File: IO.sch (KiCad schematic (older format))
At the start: 5 parts

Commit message: more updates
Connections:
- net Signaling-RINGING: no longer J?.R1
- new net Signaling-RINGDOWN: J?.R1
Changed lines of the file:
@@
 Baseband-IN
 Text GLabel 2450 2150 2    50   Output ~ 0
-Signaling-RINGING
+Signaling-RINGDOWN
 Text Notes 850  1050 0    50   ~ 0
 Audio Jack

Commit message: updates
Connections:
- net Signaling-RINGING is gone; now on net Signaling-RINGDOWN: J?.8 (Pin_8)
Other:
- note added: "Baseband Module Interface"
- note removed: "Module Interface"
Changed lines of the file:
@@
 $Descr A4 11693 8268
 encoding utf-8
-Sheet 6 10
+Sheet 6 11
 Title "300 Baud Audio FSK Modem "
 Date "2021-07-08"
@@
 	0    -1   -1   0
 $EndComp
-Text GLabel 7100 4450 2    50   Input ~ 0
+Text GLabel 7100 4450 2    50   Output ~ 0
 Baseband-IN
-Text GLabel 7100 4550 2    50   Output ~ 0
+Text GLabel 7100 4550 2    50   Input ~ 0
 Baseband-OUT
 Text GLabel 7100 4650 2    50   Input ~ 0
@@
 E&M-SG
 Text GLabel 7100 4350 2    50   Output ~ 0
-Signaling-RINGING
+Signaling-RINGDOWN
 $Comp
 L power:GND #PWR?
@@
 	1    0    0    -1
 $EndComp
-Text Notes 5200 4500 0    50   ~ 0
-Module Interface
+Text Notes 5000 4500 0    50   ~ 0
+Baseband Module Interface
 Text GLabel 2350 4450 2    50   Input ~ 0
 E&M-R

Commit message: updates
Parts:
- added J? (x2): AudioPlug4, symbol Connector:AudioPlug4
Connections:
- net Baseband-IN: now also J?.T
- net Baseband-OUT: now also J?.T
- net GND: now also J?.S, J?.S
- net Signaling-OFFHOOK: now also J?.R1
- net Signaling-RINGDOWN: now also J?.R1
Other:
- note added: "Crossover Cable Example"
- note removed: "Audio Jack"
- moved on the sheet: J?

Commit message: updates
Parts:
- J? (x2): symbol Connector:AudioPlug4 -> Connector:AudioPlug3
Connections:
- net Baseband-IN: now also J?.R, J?.R; no longer J?.T, J?.T
- net Baseband-OUT: now also J?.T; no longer J?.T
- net GND: now also J?.R2, J?.R2
- net Signaling-OFFHOOK: now also J?.T, J?.T; no longer J?.R1, J?.R1
- net Signaling-RINGDOWN: now also J?.R1; no longer J?.R1
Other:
- note added: "X"
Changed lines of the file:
@@
 RST_Request
 $Comp
-L Connector:AudioPlug4 J?
+L Connector:AudioPlug3 J?
 U 1 1 60EB32CF
-P 1850 1350
+P 1850 1400
 AR Path="/60EB32CF" Ref="J?"  Part="1"
 AR Path="/60E9D9E5/60EB32CF" Ref="J?"  Part="1"
-F 0 "J?" H 1907 1675 50  0000 C CNN
-F 1 "AudioPlug4" H 1907 1584 50  0000 C CNN
-F 2 "" H 2200 1250 50  0001 C CNN
-F 3 "~" H 2200 1250 50  0001 C CNN
-	1    1850 1350
+F 0 "J?" H 1907 1725 50  0000 C CNN
+F 1 "AudioPlug4" H 1907 1634 50  0000 C CNN
+F 2 "" H 2200 1300 50  0001 C CNN
+F 3 "~" H 2200 1300 50  0001 C CNN
+	1    1850 1400
 	1    0    0    -1
 $EndComp
@@
 L power:GND #PWR?
 U 1 1 60EB32D5
-P 2450 1250
+P 2450 1300
 AR Path="/60EB32D5" Ref="#PWR?"  Part="1"
 AR Path="/60E9D9E5/60EB32D5" Ref="#PWR?"  Part="1"
-F 0 "#PWR?" H 2450 1000 50  0001 C CNN
-F 1 "GND" V 2455 1122 50  0000 R CNN
-F 2 "" H 2450 1250 50  0001 C CNN
-F 3 "" H 2450 1250 50  0001 C CNN
-	1    2450 1250
-	0    -1   -1   0
-$EndComp
-Text GLabel 2450 1550 2    50   Output ~ 0
+F 0 "#PWR?" H 2450 1050 50  0001 C CNN
+F 1 "GND" V 2455 1172 50  0000 R CNN
+F 2 "" H 2450 1300 50  0001 C CNN
+F 3 "" H 2450 1300 50  0001 C CNN
+	1    2450 1300
+	0    -1   -1   0
+$EndComp
+Text GLabel 2450 1500 2    50   Output ~ 0
 Baseband-OUT
-Text GLabel 2450 1450 2    50   Output ~ 0
+Text GLabel 2450 2400 2    50   Output ~ 0
 Signaling-OFFHOOK
 Wire Notes Line
@@
 	8000 4250 3800 4250
 $Comp
-L Connector:AudioPlug4 J?
+L Connector:AudioPlug3 J?
 U 1 1 60EE43AB
-P 5900 1350
+P 5900 1400
 AR Path="/60EE43AB" Ref="J?"  Part="1"
 AR Path="/60E9D9E5/60EE43AB" Ref="J?"  Part="1"
-F 0 "J?" H 5957 1675 50  0000 C CNN
-F 1 "AudioPlug4" H 5957 1584 50  0000 C CNN
-F 2 "" H 6250 1250 50  0001 C CNN
-F 3 "~" H 6250 1250 50  0001 C CNN
-	1    5900 1350
+F 0 "J?" H 5957 1725 50  0000 C CNN
+F 1 "AudioPlug4" H 5957 1634 50  0000 C CNN
+F 2 "" H 6250 1300 50  0001 C CNN
+F 3 "~" H 6250 1300 50  0001 C CNN
+	1    5900 1400
 	-1   0    0    -1
 $EndComp
@@
 L power:GND #PWR?
 U 1 1 60EE44F5
-P 5300 1250
+P 5300 1300
 AR Path="/60EE44F5" Ref="#PWR?"  Part="1"
 AR Path="/60E9D9E5/60EE44F5" Ref="#PWR?"  Part="1"
-F 0 "#PWR?" H 5300 1000 50  0001 C CNN
-F 1 "GND" V 5305 1122 50  0000 R CNN
-F 2 "" H 5300 1250 50  0001 C CNN
-F 3 "" H 5300 1250 50  0001 C CNN
-	1    5300 1250
+F 0 "#PWR?" H 5300 1050 50  0001 C CNN
+F 1 "GND" V 5305 1172 50  0000 R CNN
+F 2 "" H 5300 1300 50  0001 C CNN
+F 3 "" H 5300 1300 50  0001 C CNN
+	1    5300 1300
 	0    1    -1   0
 $EndComp
-Text GLabel 5300 1550 0    50   Input ~ 0
+Text GLabel 5300 1400 0    50   Input ~ 0
 Baseband-IN
-Text GLabel 5300 1450 0    50   Input ~ 0
+Text GLabel 5300 2300 0    50   Input ~ 0
 Signaling-RINGDOWN
 Text Notes 3250 1000 0    50   ~ 0
@@
 	0    -1   -1   0
 $EndComp
+Text GLabel 5300 1500 0    50   Output ~ 0
+Baseband-OUT
 Text GLabel 5300 2400 0    50   Output ~ 0
-Baseband-OUT
-Text GLabel 5300 2300 0    50   Output ~ 0
 Signaling-OFFHOOK
 $Comp
@@
 	0    1    -1   0
 $EndComp
-Text GLabel 2450 2400 2    50   Input ~ 0
+Text GLabel 2450 1400 2    50   Input ~ 0
 Baseband-IN
 Text GLabel 2450 2300 2    50   Input ~ 0
@@
 Wire Notes Line
 	2200 2600 2200 1900
+Text Notes 3800 1450 0    50   ~ 0
+X
+$Comp
+L power:GND #PWR?
+U 1 1 60ECC43D
+P 2450 2200
+AR Path="/60ECC43D" Ref="#PWR?"  Part="1"
+AR Path="/60E9D9E5/60ECC43D" Ref="#PWR?"  Part="1"
+F 0 "#PWR?" H 2450 1950 50  0001 C CNN
+F 1 "GND" V 2455 2072 50  0000 R CNN
+F 2 "" H 2450 2200 50  0001 C CNN
+F 3 "" H 2450 2200 50  0001 C CNN
+	1    2450 2200
+	0    -1   -1   0
+$EndComp
+$Comp
+L power:GND #PWR?
+U 1 1 60ECC77D
+P 5300 2200
+AR Path="/60ECC77D" Ref="#PWR?"  Part="1"
+AR Path="/60E9D9E5/60ECC77D" Ref="#PWR?"  Part="1"
+F 0 "#PWR?" H 5300 1950 50  0001 C CNN
+F 1 "GND" V 5305 2072 50  0000 R CNN
+F 2 "" H 5300 2200 50  0001 C CNN
+F 3 "" H 5300 2200 50  0001 C CNN
+	1    5300 2200
+	0    1    -1   0
+$EndComp
+Text Notes 3800 2400 0    50   ~ 0
+X
 $EndSCHEMATC

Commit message: io interface updates
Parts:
- added J?: Conn_01x08_Male, symbol Connector_Generic:Conn_01x08
- added J?: Conn_02x10_Odd_Even, symbol Connector_Generic:Conn_02x10_Odd_Even
- added J? (x2): AudioJack4, symbol Connector:AudioJack4
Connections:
- net +5V: now also J?.1 (Pin_1), J?.2 (Pin_2)
- net Baseband-IN: now also J?.10 (Pin_10)
- net Baseband-OUT: now also J?.12 (Pin_12)
- net E&M-E: no longer J?.7, J?.7 (Pin_7)
- net E&M-M: no longer J?.2, J?.2 (Pin_2)
- net E&M-R: no longer J?.4, J?.4 (Pin_4)
- net E&M-R1: no longer J?.3, J?.3 (Pin_3)
- net E&M-SB: no longer J?.1, J?.1 (Pin_1)
- net E&M-SG: no longer J?.8, J?.8 (Pin_8)
- net E&M-T: no longer J?.5, J?.5 (Pin_5)
- net E&M-T1: no longer J?.6, J?.6 (Pin_6)
- net GND: now also J?.19 (Pin_19), J?.20 (Pin_20)
- net I2C-SDA: now also J?.18 (Pin_18)
- net I2C-SDL: now also J?.16 (Pin_16)
- net RST_Request: now also J?.4 (Pin_4)
- net Signaling-OFFHOOK: now also J?.14 (Pin_14)
- net Signaling-RINGDOWN: now also J?.8 (Pin_8)
- net TTL-CTS: now also J?.13 (Pin_13)
- net TTL-DCD: now also J?.15 (Pin_15)
- net TTL-DSR: now also J?.17 (Pin_17)
- net TTL-DTR: now also J?.3 (Pin_3)
- net TTL-RI: now also J?.5 (Pin_5)
- net TTL-RTS: now also J?.7 (Pin_7)
- net TTL-RX: now also J?.9 (Pin_9)
- net TTL-TX: now also J?.11 (Pin_11)
- new net: J?.1, J?.1 (Pin_1)
- new net: J?.2, J?.2 (Pin_2)
- new net: J?.3, J?.3 (Pin_3)
- new net: J?.4, J?.4 (Pin_4)
- new net: J?.5, J?.5 (Pin_5)
- new net: J?.6, J?.6 (Pin_6)
- new net: J?.7, J?.7 (Pin_7)
- new net: J?.8, J?.8 (Pin_8)
- new net: J?.1 (Pin_1), J?.T
- new net: J?.2 (Pin_2), J?.R1
- new net: J?.3 (Pin_3), J?.R2
- new net: J?.4 (Pin_4), J?.S
- new net: J?.5 (Pin_5), J?.S
- new net: J?.6 (Pin_6), J?.R2
- new net: J?.7 (Pin_7), J?.R1
- new net: J?.8 (Pin_8), J?.T
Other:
- note added: "2xTRRS Module Interface\nBASEBAND"
- note added: "RJ45 Module Interface\nTELEPHONY"
- note removed: "Baseband Module Interface"
- moved on the sheet: J?

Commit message: updates
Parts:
- removed J? (x2): AudioPlug4, symbol Connector:AudioPlug3
- added J? (x2): AudioPlug4, symbol Connector:AudioPlug4
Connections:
- net +5V: no longer J?.2 (Pin_2), J?.2 (Pin_2)
- net Baseband-IN: now also J?.8 (Pin_8), J?.8 (Pin_8), J?.R1, J?.T; no longer J?.10 (Pin_10), J?.10 (Pin_10)
- net Baseband-OUT: now also J?.10 (Pin_10), J?.10 (Pin_10), J?.R1, J?.T; no longer J?.12 (Pin_12), J?.12 (Pin_12)
- net GND: now also J?.R2, J?.R2, J?.S, J?.S; no longer J?.19 (Pin_19), J?.19 (Pin_19)
- net I2C-SDA: now also J?.16 (Pin_16), J?.16 (Pin_16); no longer J?.18 (Pin_18), J?.18 (Pin_18)
- net I2C-SDL: now also J?.14 (Pin_14), J?.14 (Pin_14); no longer J?.16 (Pin_16), J?.16 (Pin_16)
- net RST_Request: now also J?.2 (Pin_2), J?.2 (Pin_2); no longer J?.4 (Pin_4), J?.4 (Pin_4)
- net Signaling-OFFHOOK: now also J?.12 (Pin_12), J?.12 (Pin_12); no longer J?.14 (Pin_14), J?.14 (Pin_14)
- net Signaling-RINGDOWN: now also J?.6 (Pin_6), J?.6 (Pin_6); no longer J?.8 (Pin_8), J?.8 (Pin_8)
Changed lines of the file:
@@
-$EndComp
-$Comp
-L power:GND #PWR?
-U 1 1 60EA1224
-P 6550 6100
-AR Path="/60EA1224" Ref="#PWR?"  Part="1"
-AR Path="/60E9D9E5/60EA1224" Ref="#PWR?"  Part="1"
-F 0 "#PWR?" H 6550 5850 50  0001 C CNN
-F 1 "GND" V 6555 5972 50  0000 R CNN
-F 2 "" H 6550 6100 50  0001 C CNN
-F 3 "" H 6550 6100 50  0001 C CNN
-	1    6550 6100
-	0    1    1    0
-$EndComp
-$Comp
-L power:+5V #PWR?
-U 1 1 60EA122A
-P 7050 5200
-AR Path="/60EA122A" Ref="#PWR?"  Part="1"
-AR Path="/60E9D9E5/60EA122A" Ref="#PWR?"  Part="1"
-F 0 "#PWR?" H 7050 5050 50  0001 C CNN
-F 1 "+5V" V 7065 5328 50  0000 L CNN
-F 2 "" H 7050 5200 50  0001 C CNN
-F 3 "" H 7050 5200 50  0001 C CNN
-	1    7050 5200
-	0    1    1    0
 $EndComp
 $Comp
@@
 Text Notes 4900 3650 0    50   ~ 0
 2xTRRS Module Interface\nBASEBAND
-Text GLabel 7050 5300 2    50   Output ~ 0
+Text GLabel 7050 5200 2    50   Output ~ 0
 RST_Request
-$Comp
-L Connector:AudioPlug3 J?
-U 1 1 60EB32CF
-P 3900 1250
-AR Path="/60EB32CF" Ref="J?"  Part="1"
-AR Path="/60E9D9E5/60EB32CF" Ref="J?"  Part="1"
-F 0 "J?" H 3957 1575 50  0000 C CNN
-F 1 "AudioPlug4" H 3957 1484 50  0000 C CNN
-F 2 "" H 4250 1150 50  0001 C CNN
-F 3 "~" H 4250 1150 50  0001 C CNN
-	1    3900 1250
-	1    0    0    -1
-$EndComp
 $Comp
 L power:GND #PWR?
@@
 	0    -1   -1   0
 $EndComp
-Text GLabel 4500 1350 2    50   Output ~ 0
+Text GLabel 4500 1450 2    50   Output ~ 0
 Baseband-OUT
 Text GLabel 4500 2250 2    50   Output ~ 0
@@
 Wire Notes Line
 	8050 6350 8050 4800
-$Comp
-L Connector:AudioPlug3 J?
-U 1 1 60EE43AB
-P 7950 1250
-AR Path="/60EE43AB" Ref="J?"  Part="1"
-AR Path="/60E9D9E5/60EE43AB" Ref="J?"  Part="1"
-F 0 "J?" H 8007 1575 50  0000 C CNN
-F 1 "AudioPlug4" H 8007 1484 50  0000 C CNN
-F 2 "" H 8300 1150 50  0001 C CNN
-F 3 "~" H 8300 1150 50  0001 C CNN
-	1    7950 1250
-	-1   0    0    -1
-$EndComp
 $Comp
 L power:GND #PWR?
@@
 	0    1    -1   0
 $EndComp
-Text GLabel 7350 1250 0    50   Input ~ 0
+Text GLabel 7350 1450 0    50   Input ~ 0
 Baseband-IN
 Text GLabel 7350 2150 0    50   Input ~ 0
@@
 Text Notes 5300 850  0    50   ~ 0
 Crossover Cable Example
-Text GLabel 7050 6000 2    50   Input ~ 0
+Text GLabel 7050 5900 2    50   Input ~ 0
 I2C-SDA
-Text GLabel 7050 5900 2    50   Input ~ 0
+Text GLabel 7050 5800 2    50   Input ~ 0
 I2C-SDL
 $Comp
@@
 	0    -1   -1   0
 $EndComp
+Text GLabel 7050 5400 2    50   Output ~ 0
+Signaling-RINGDOWN
+Text GLabel 7050 5700 2    50   Input ~ 0
+Signaling-OFFHOOK
+Text GLabel 7050 5600 2    50   Input ~ 0
+Baseband-OUT
 Text GLabel 7050 5500 2    50   Output ~ 0
-Signaling-RINGDOWN
-Text GLabel 7050 5800 2    50   Input ~ 0
-Signaling-OFFHOOK
-Text GLabel 7050 5700 2    50   Input ~ 0
-Baseband-OUT
-Text GLabel 7050 5600 2    50   Output ~ 0
 Baseband-IN
 $Comp
@@
 	0    1    -1   0
 $EndComp
-Text GLabel 4500 1250 2    50   Input ~ 0
+Text GLabel 4500 1350 2    50   Input ~ 0
 Baseband-IN
 Text GLabel 4500 2150 2    50   Input ~ 0
@@
 	4250 2450 7600 2450
 Wire Notes Line
-	4250 900  7600 900
+	4250 950  7600 950
 Wire Notes Line
 	4250 1600 7600 1600
@@
 	1    3900 3750
 	1    0    0    1
-$EndComp
-$Comp
-L power:GND #PWR?
-U 1 1 60F6E687
-P 6550 4150
-AR Path="/60F6E687" Ref="#PWR?"  Part="1"
-AR Path="/60E9D9E5/60F6E687" Ref="#PWR?"  Part="1"
-F 0 "#PWR?" H 6550 3900 50  0001 C CNN
-F 1 "GND" V 6555 4022 50  0000 R CNN
-F 2 "" H 6550 4150 50  0001 C CNN
-F 3 "" H 6550 4150 50  0001 C CNN
-	1    6550 4150
-	0    1    1    0
-$EndComp
-$Comp
-L power:+5V #PWR?
-U 1 1 60F6E691
-P 7050 3250
-AR Path="/60F6E691" Ref="#PWR?"  Part="1"
-AR Path="/60E9D9E5/60F6E691" Ref="#PWR?"  Part="1"
-F 0 "#PWR?" H 7050 3100 50  0001 C CNN
-F 1 "+5V" V 7065 3378 50  0000 L CNN
-F 2 "" H 7050 3250 50  0001 C CNN
-F 3 "" H 7050 3250 50  0001 C CNN
-	1    7050 3250
-	0    1    1    0
 $EndComp
 $Comp
@@
 Text Notes 5050 5650 0    50   ~ 0
 RJ45 Module Interface\nTELEPHONY
-Text GLabel 7050 3350 2    50   Output ~ 0
+Text GLabel 7050 3250 2    50   Output ~ 0
 RST_Request
 Wire Notes Line
 	8050 2800 3850 2800
-Text GLabel 7050 4050 2    50   Input ~ 0
+Text GLabel 7050 3950 2    50   Input ~ 0
 I2C-SDA
-Text GLabel 7050 3950 2    50   Input ~ 0
+Text GLabel 7050 3850 2    50   Input ~ 0
 I2C-SDL
 $Comp
@@
 	0    -1   -1   0
 $EndComp
+Text GLabel 7050 3450 2    50   Output ~ 0
+Signaling-RINGDOWN
+Text GLabel 7050 3750 2    50   Input ~ 0
+Signaling-OFFHOOK
+Text GLabel 7050 3650 2    50   Input ~ 0
+Baseband-OUT
 Text GLabel 7050 3550 2    50   Output ~ 0
-Signaling-RINGDOWN
-Text GLabel 7050 3850 2    50   Input ~ 0
-Signaling-OFFHOOK
-Text GLabel 7050 3750 2    50   Input ~ 0
-Baseband-OUT
-Text GLabel 7050 3650 2    50   Output ~ 0
 Baseband-IN
 $Comp
@@
 Wire Notes Line
 	8050 2800 8050 4500
+$Comp
+L Connector:AudioPlug4 J?
+U 1 1 60FDB7A8
+P 3900 1250
+AR Path="/60FDB7A8" Ref="J?"  Part="1"
+AR Path="/60E9D9E5/60FDB7A8" Ref="J?"  Part="1"
+F 0 "J?" H 3957 1575 50  0000 C CNN
+F 1 "AudioPlug4" H 3957 1484 50  0000 C CNN
+F 2 "" H 4250 1150 50  0001 C CNN
+F 3 "~" H 4250 1150 50  0001 C CNN
+	1    3900 1250
+	1    0    0    -1
+$EndComp
+$Comp
+L Connector:AudioPlug4 J?
+U 1 1 60FDC067
+P 7950 1250
+AR Path="/60FDC067" Ref="J?"  Part="1"
+AR Path="/60E9D9E5/60FDC067" Ref="J?"  Part="1"
+F 0 "J?" H 8007 1575 50  0000 C CNN
+F 1 "AudioPlug4" H 8007 1484 50  0000 C CNN
+F 2 "" H 8300 1150 50  0001 C CNN
+F 3 "~" H 8300 1150 50  0001 C CNN
+	1    7950 1250
+	-1   0    0    -1
+$EndComp
+$Comp
+L power:GND #PWR?
+U 1 1 60FE2765
+P 4500 1250
+AR Path="/60FE2765" Ref="#PWR?"  Part="1"
+AR Path="/60E9D9E5/60FE2765" Ref="#PWR?"  Part="1"
+F 0 "#PWR?" H 4500 1000 50  0001 C CNN
+F 1 "GND" V 4505 1122 50  0000 R CNN
+F 2 "" H 4500 1250 50  0001 C CNN
+F 3 "" H 4500 1250 50  0001 C CNN
+	1    4500 1250
+	0    -1   -1   0
+$EndComp
+$Comp
+L power:GND #PWR?
+U 1 1 60FE2987
+P 7350 1250
+AR Path="/60FE2987" Ref="#PWR?"  Part="1"
+AR Path="/60E9D9E5/60FE2987" Ref="#PWR?"  Part="1"
+F 0 "#PWR?" H 7350 1000 50  0001 C CNN
+F 1 "GND" V 7355 1122 50  0000 R CNN
+F 2 "" H 7350 1250 50  0001 C CNN
+F 3 "" H 7350 1250 50  0001 C CNN
+	1    7350 1250
+	0    1    -1   0
+$EndComp
 $EndSCHEMATC

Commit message: general updates
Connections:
- net I2C-SDA: now also J?.18 (Pin_18), J?.18 (Pin_18); no longer J?.16 (Pin_16), J?.16 (Pin_16)
- net I2C-SDL: now also J?.16 (Pin_16), J?.16 (Pin_16); no longer J?.14 (Pin_14), J?.14 (Pin_14)
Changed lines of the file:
@@
 $Descr A4 11693 8268
 encoding utf-8
-Sheet 6 11
+Sheet 6 12
 Title "300 Baud Audio FSK Modem "
 Date "2021-07-08"
@@
 Text Notes 5300 850  0    50   ~ 0
 Crossover Cable Example
+Text GLabel 7050 6000 2    50   Input ~ 0
+I2C-SDA
 Text GLabel 7050 5900 2    50   Input ~ 0
-I2C-SDA
-Text GLabel 7050 5800 2    50   Input ~ 0
 I2C-SDL
 $Comp
@@
 Wire Notes Line
 	8050 2800 3850 2800
+Text GLabel 7050 4050 2    50   Input ~ 0
+I2C-SDA
 Text GLabel 7050 3950 2    50   Input ~ 0
-I2C-SDA
-Text GLabel 7050 3850 2    50   Input ~ 0
 I2C-SDL
 $Comp

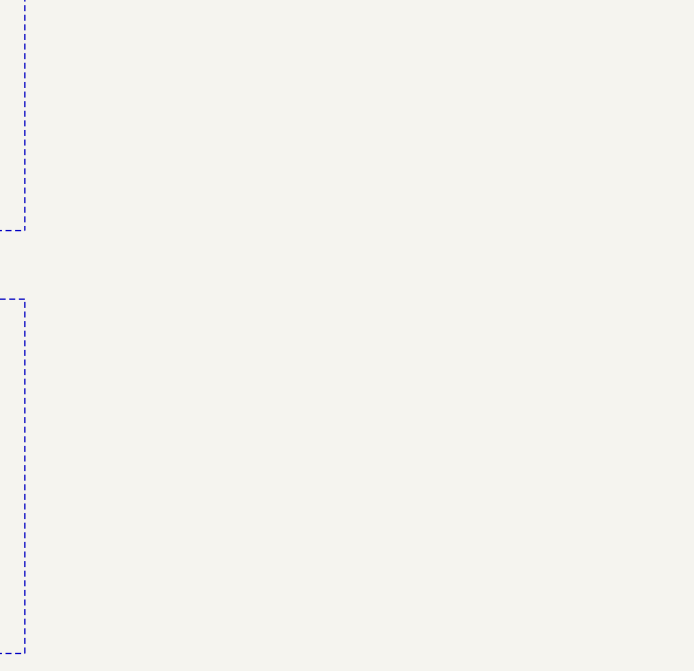
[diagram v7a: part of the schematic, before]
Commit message: added kenwood 2pin
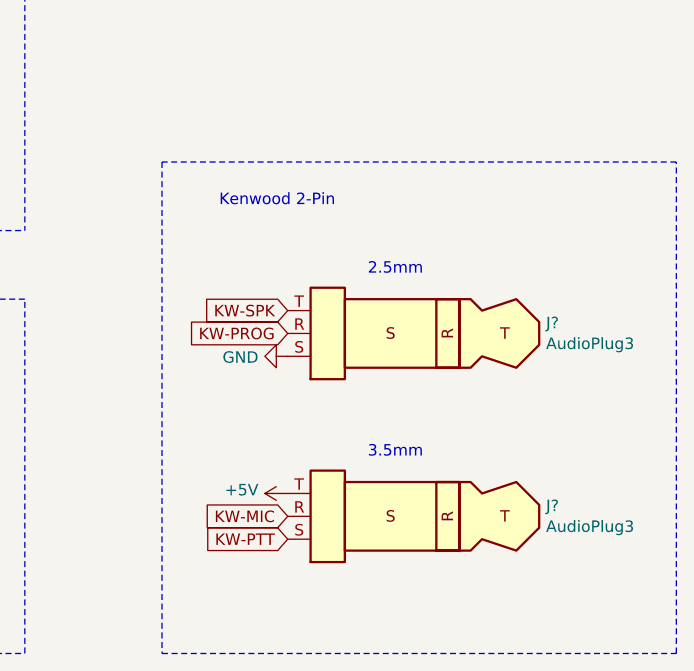
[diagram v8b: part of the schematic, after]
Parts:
- added J? (x2): AudioPlug3, symbol Connector:AudioPlug3
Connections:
- net +5V: now also J?.T
- net GND: now also J?.S
- new net KW-MIC: J?.R
- new net KW-PROG: J?.R
- new net KW-PTT: J?.S
- new net KW-SPK: J?.T
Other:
- note added: "2.5mm"
- note added: "3.5mm"
- note added: "Kenwood 2-Pin"
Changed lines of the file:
@@
 	0    1    -1   0
 $EndComp
+$Comp
+L Connector:AudioPlug3 J?
+U 1 1 6101043E
+P 9800 4950
+F 0 "J?" H 9270 4904 50  0000 R CNN
+F 1 "AudioPlug3" H 9270 4995 50  0000 R CNN
+F 2 "" H 9900 4900 50  0001 C CNN
+F 3 "~" H 9900 4900 50  0001 C CNN
+	1    9800 4950
+	-1   0    0    1
+$EndComp
+$Comp
+L Connector:AudioPlug3 J?
+U 1 1 61011A7F
+P 9800 5750
+F 0 "J?" H 9270 5704 50  0000 R CNN
+F 1 "AudioPlug3" H 9270 5795 50  0000 R CNN
+F 2 "" H 9900 5700 50  0001 C CNN
+F 3 "~" H 9900 5700 50  0001 C CNN
+	1    9800 5750
+	-1   0    0    1
+$EndComp
+Text Notes 8900 4400 0    50   ~ 0
+Kenwood 2-Pin
+Wire Notes Line
+	8650 4200 8650 6350
+Wire Notes Line
+	8650 6350 10900 6350
+Wire Notes Line
+	10900 6350 10900 4200
+Wire Notes Line
+	10900 4200 8650 4200
+Text GLabel 9200 4950 0    50   Input ~ 0
+KW-PROG
+$Comp
+L power:GND #PWR?
+U 1 1 61017F92
+P 9200 5050
+AR Path="/61017F92" Ref="#PWR?"  Part="1"
+AR Path="/60E9D9E5/61017F92" Ref="#PWR?"  Part="1"
+F 0 "#PWR?" H 9200 4800 50  0001 C CNN
+F 1 "GND" V 9205 4922 50  0000 R CNN
+F 2 "" H 9200 5050 50  0001 C CNN
+F 3 "" H 9200 5050 50  0001 C CNN
+	1    9200 5050
+	0    1    1    0
+$EndComp
+$Comp
+L power:+5V #PWR?
+U 1 1 610186A8
+P 9200 5650
+AR Path="/610186A8" Ref="#PWR?"  Part="1"
+AR Path="/60E9D9E5/610186A8" Ref="#PWR?"  Part="1"
+F 0 "#PWR?" H 9200 5500 50  0001 C CNN
+F 1 "+5V" V 9215 5778 50  0000 L CNN
+F 2 "" H 9200 5650 50  0001 C CNN
+F 3 "" H 9200 5650 50  0001 C CNN
+	1    9200 5650
+	0    -1   -1   0
+$EndComp
+Text Notes 9550 5500 0    50   ~ 0
+3.5mm
+Text Notes 9550 4700 0    50   ~ 0
+2.5mm
+Text GLabel 9200 4850 0    50   Input ~ 0
+KW-SPK
+Text GLabel 9200 5750 0    50   Input ~ 0
+KW-MIC
+Text GLabel 9200 5850 0    50   Input ~ 0
+KW-PTT
 $EndSCHEMATC
